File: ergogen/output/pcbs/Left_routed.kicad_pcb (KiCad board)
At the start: 2 copper layers, 130.3 x 105.3 mm, 44 parts

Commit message: update config
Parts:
- MCU1: footprint 1:xiao_smd_xl_cutout -> 1:xiao_smd_xl_cutout_minimal
- SW1: footprint power_switch -> 1208YD
- moved SW1 58.6 mm to (175.2, 34.2), turned to 0 degrees
- moved S19 58.0 mm to (118.2, 31.4)
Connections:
- MCU1 pad 17: GND -> RST
- SW1 pad 1: (no net) -> BAT
- SW1 pad 2: BAT -> BAT_CONN
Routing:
- net BAT_CONN: track 74.3 -> 145.6 mm
- net GND: track 153.0 -> 87.2 mm
- net RST: track 85.7 -> 28.9 mm
- net BAT: track 29.9 -> 79.5 mm
- net pinky_home: track 12.2 -> 13.8 mm
- net pinky_top: track 12.2 -> 13.7 mm
- net C4: track 154.6 -> 156.1 mm
- net C3: track 132.2 -> 133.5 mm
- net pinky_bottom: track 12.4 -> 13.7 mm
- net base_cluster: track 13.8 -> 12.5 mm
- net extension_cluster: track 13.5 -> 12.4 mm
- net C2: track 110.4 -> 111.4 mm
- net flexion_cluster: track 13.3 -> 12.3 mm
- net C1: track 49.8 -> 50.4 mm
- net ring_home: track 13.1 -> 13.7 mm
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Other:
- board size 130.3 x 105.3 mm -> 130 x 105 mm
- board text added: "2024.10.12"
- board text added: "liaison"
- board text removed: "JLCJLCJLCJLC"
- board text removed: "ON"
- board text removed: "alias"
- board text removed: "v2"

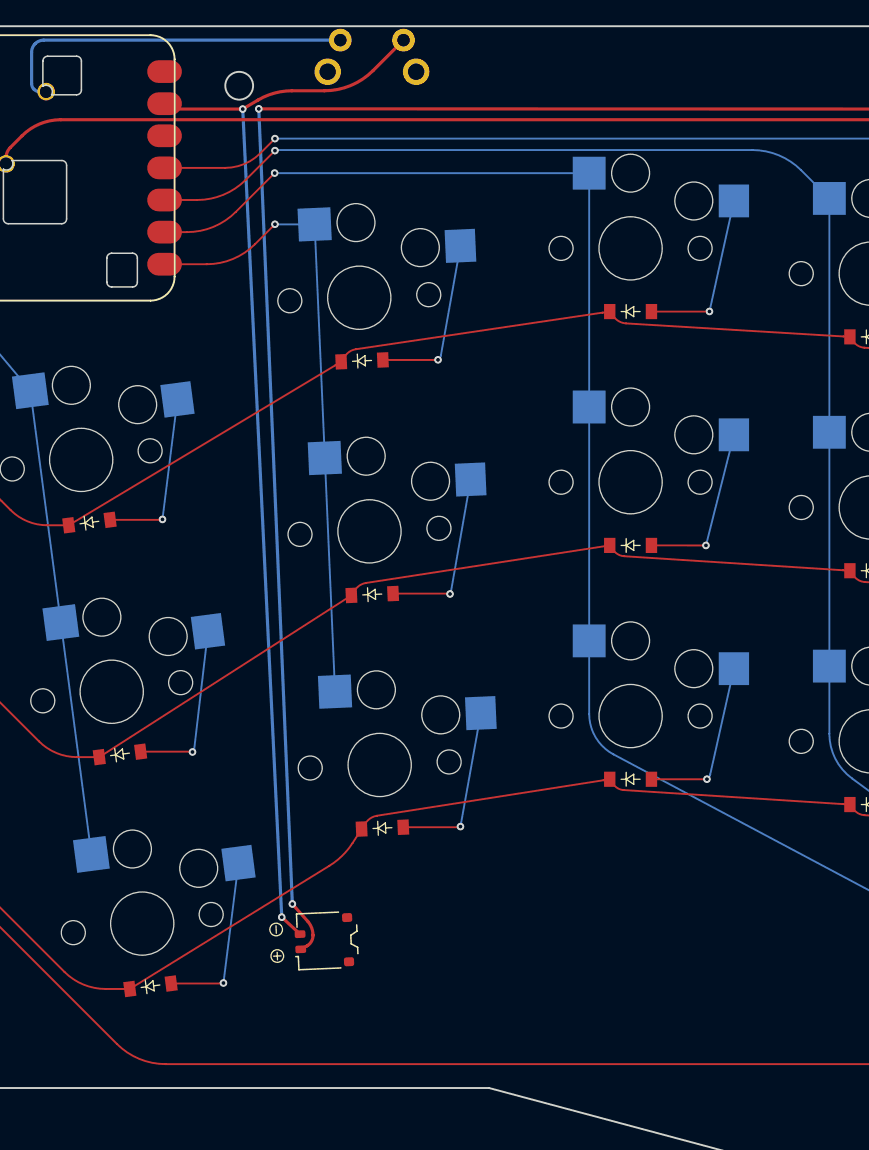
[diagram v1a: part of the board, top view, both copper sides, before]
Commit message: add battery outlines to pcb
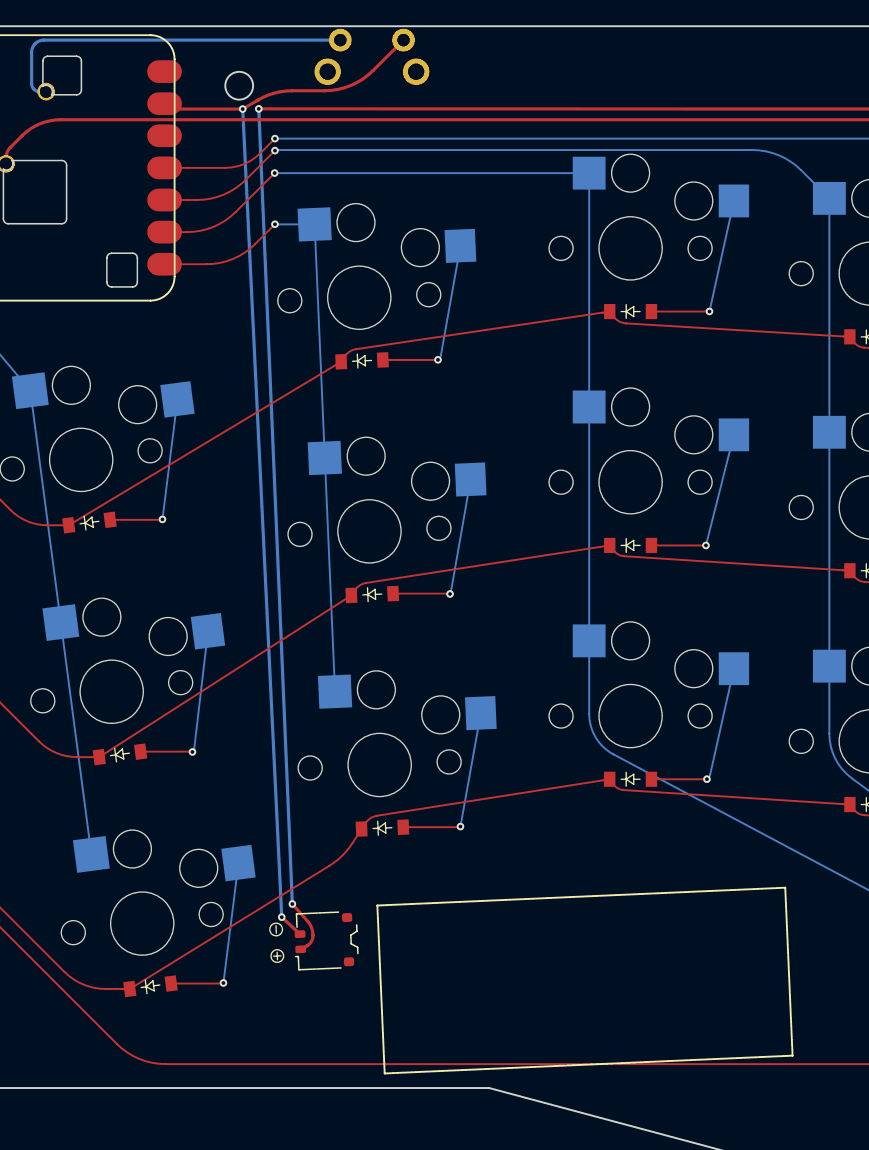
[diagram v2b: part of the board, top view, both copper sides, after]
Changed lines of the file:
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@@
 		(fp_arc
 			(start 1.136553 -8.832047)
-			(mid 1.405961 -8.720454)
+			(mid 1.405958 -8.720453)
 			(end 1.517553 -8.451047)
 			(stroke
@@
 	)
 	(gr_line
+		(start 118.599764 98.570467)
+		(end 119.179902 111.857809)
+		(stroke
+			(width 0.15)
+			(type default)
+		)
+		(layer "F.SilkS")
+	)
+	(gr_line
+		(start 151.44916 110.448903)
+		(end 150.869022 97.161561)
+		(stroke
+			(width 0.15)
+			(type default)
+		)
+		(layer "F.SilkS")
+	)
+	(gr_line
+		(start 119.179902 111.857809)
+		(end 151.44916 110.448903)
+		(stroke
+			(width 0.15)
+			(type default)
+		)
+		(layer "F.SilkS")
+	)
+	(gr_line
+		(start 150.869022 97.161561)
+		(end 118.599764 98.570467)
+		(stroke
+			(width 0.15)
+			(type default)
+		)
+		(layer "F.SilkS")
+	)
+	(gr_line
 		(start 127.44412 113.00854)
 		(end 205.849729 134.01726)
@@
 		)
 	)
+	(group ""
+		(members "0ce6c5f5-ebda-47d3-aa48-854b242e355f" "63e7ba3a-4356-4589-9a90-e1ea7ff0bcab"
+			"ef7c0747-e612-4180-8c9e-a8d90d05828c" "fb0eaee8-3399-46e0-811b-12d0a07ccac9"
+		)
+	)
